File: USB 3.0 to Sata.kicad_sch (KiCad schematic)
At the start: 34 parts, among them J1 USB_C_Receptacle, U3 VL716-Q4, U4 XUTS-2205-0429, U5 W25Q16BVSSIG, Y2 25Mhz Crystal

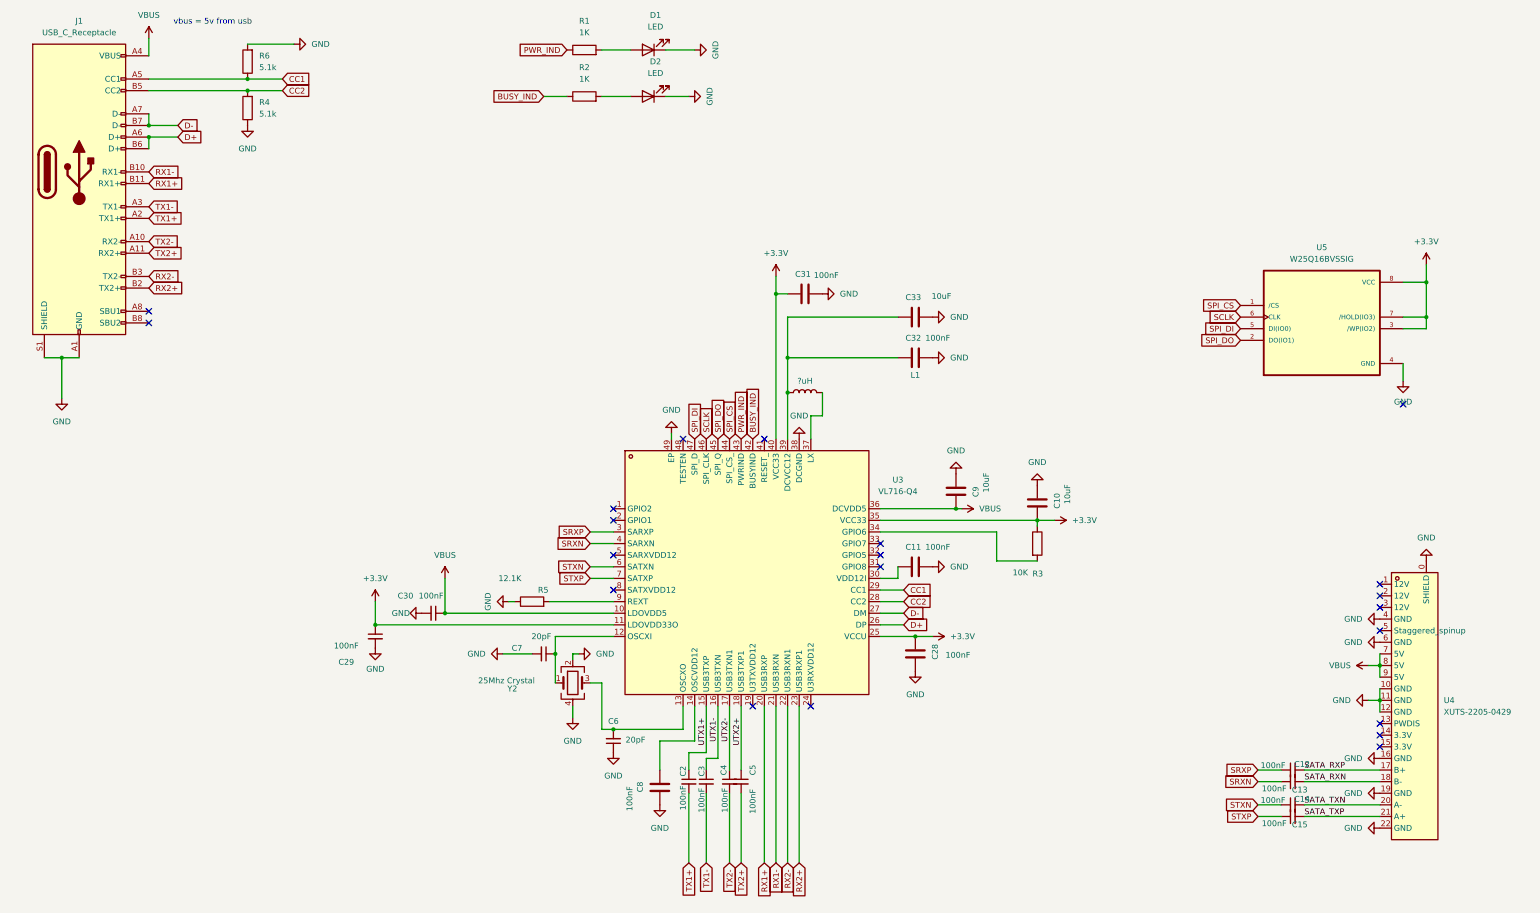
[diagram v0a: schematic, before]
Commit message: Fixed pcb errors
Fixed RX2 TX2 lines being flipped, changed usb port footprint to the corect one, changed flash footprint from SOP8-150MIL to SOP8-208MIL
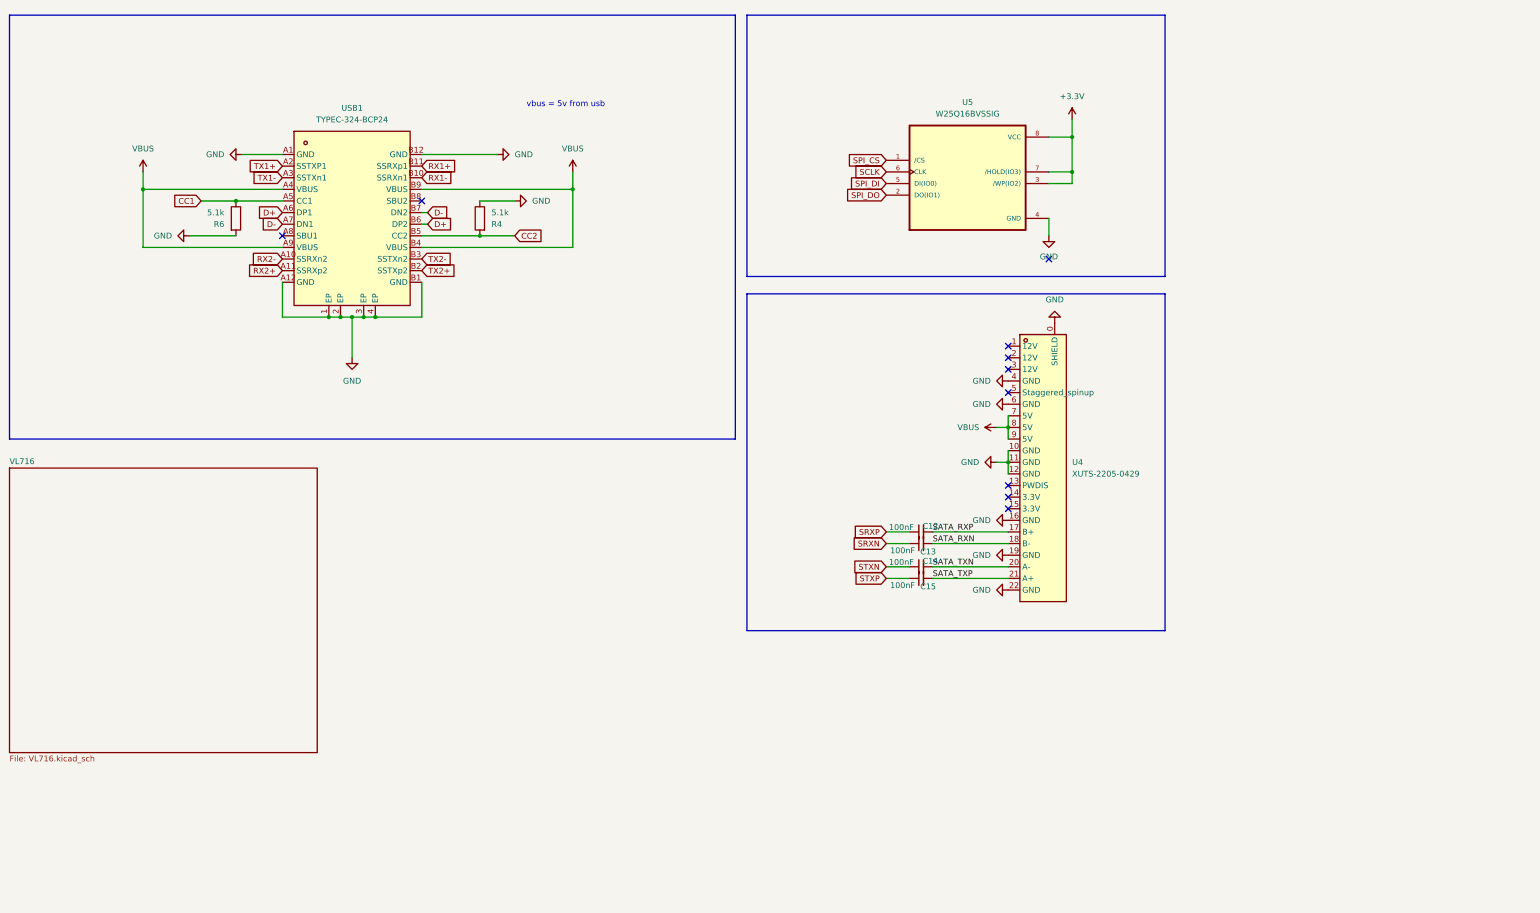
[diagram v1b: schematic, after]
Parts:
- removed C10, C33, C9: 10uF, Capacitor_SMD:C_0805_2012Metric, symbol Device:C
- removed C11, C28, C31, C32, C8: 100nF, Capacitor_SMD:C_0402_1005Metric, symbol Device:C
- removed C2, C29, C3, C30, C4, C5: 100nF, Capacitor_SMD:C_0402_1005Metric, symbol Device:C_Small
- removed C6, C7: 20pF, Capacitor_SMD:C_0402_1005Metric, symbol Device:C_Small
- removed D1, D2: LED, LED_SMD:LED_0603_1608Metric, symbol Device:LED
- removed J1: USB_C_Receptacle, Connector_USB:USB_C_Receptacle_Amphenol_12401548E4-2A, symbol Connector:USB_C_Receptacle
- removed L1: ?uH, Inductor_SMD:L_Cenker_CKCS5040, symbol Device:L
- removed R1, R2: 1K, Resistor_SMD:R_0402_1005Metric, symbol Device:R
- removed R3: 10K, Resistor_SMD:R_0402_1005Metric, symbol Device:R
- removed R5: 12.1K, Resistor_SMD:R_0402_1005Metric, symbol Device:R
- removed U3: VL716-Q4, da:QFN-48_L6.0-W6.0-P0.40-BL-EP3.8, symbol da:VL716-Q4
- removed Y2: 25Mhz Crystal, Crystal:Crystal_SMD_3225-4Pin_3.2x2.5mm, symbol Device:Crystal_GND24
- added USB1: TYPEC-324-BCP24, da:USB-C-SMD_TYPEC-324-BCP24, symbol da:TYPEC-324-BCP24
- U5: footprint da:SOIC-8_L5.0-W4.0-P1.27-LS6.0-BL -> da:SOIC-8_L5.3-W5.3-P1.27-LS8.0-BL
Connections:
- net CC1: now also USB1.A5 (CC1)
- net CC2: now also USB1.B5 (CC2)
- net D+: now also USB1.A6 (DP1), USB1.B6 (DP2)
- net D-: now also USB1.A7 (DN1), USB1.B7 (DN2)
- net GND: now also USB1.1 (EP), USB1.2 (EP), USB1.3 (EP), USB1.4 (EP), USB1.A1 (GND), USB1.A12 (GND), USB1.B1 (GND), USB1.B12 (GND)
- net RX1+: now also USB1.B11 (SSRXp1)
- net RX1-: now also USB1.B10 (SSRXn1)
- net RX2+: now also USB1.A11 (SSRXp2)
- net RX2-: now also USB1.A10 (SSRXn2)
- net TX1+: now also USB1.A2 (SSTXP1)
- net TX1-: now also USB1.A3 (SSTXn1)
- net TX2+: now also USB1.B2 (SSTXp2)
- net TX2-: now also USB1.B3 (SSTXn2)
- net VBUS: now also USB1.A4 (VBUS), USB1.A9 (VBUS), USB1.B4 (VBUS), USB1.B9 (VBUS)
- no-connect marks 21 -> 10
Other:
- added sheet VL716 (VL716.kicad_sch)
- moved on the sheet: C12, C13, C14, C15, R4, R6, U4, U5

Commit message: .
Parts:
- added C21, C22: 22uF, Capacitor_SMD:C_0805_2012Metric, symbol Device:C
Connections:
- net GND: now also C21.2, C22.2
- net VBUS: now also C21.1, C22.1
